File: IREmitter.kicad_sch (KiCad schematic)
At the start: 0 parts

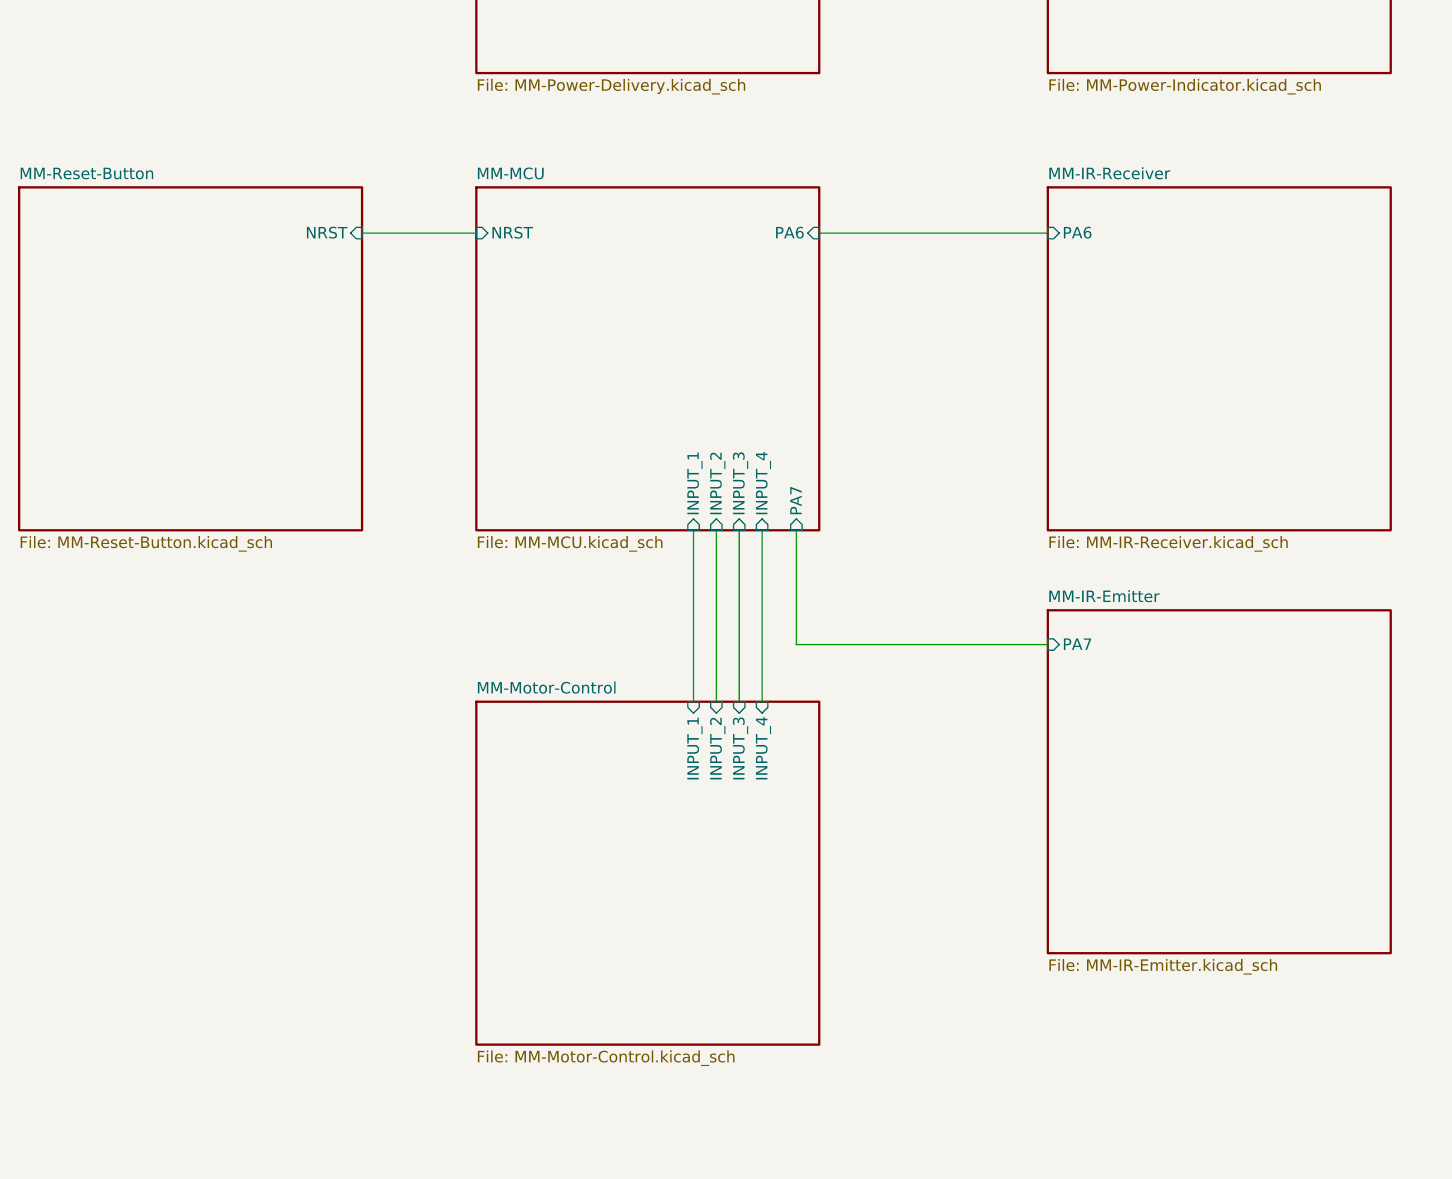
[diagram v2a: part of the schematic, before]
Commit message: redid the 4 emitters receivers, fixed orientation of LEDS and going to continue adding footprints and replace the 60ohm resistors with 300ohm ones
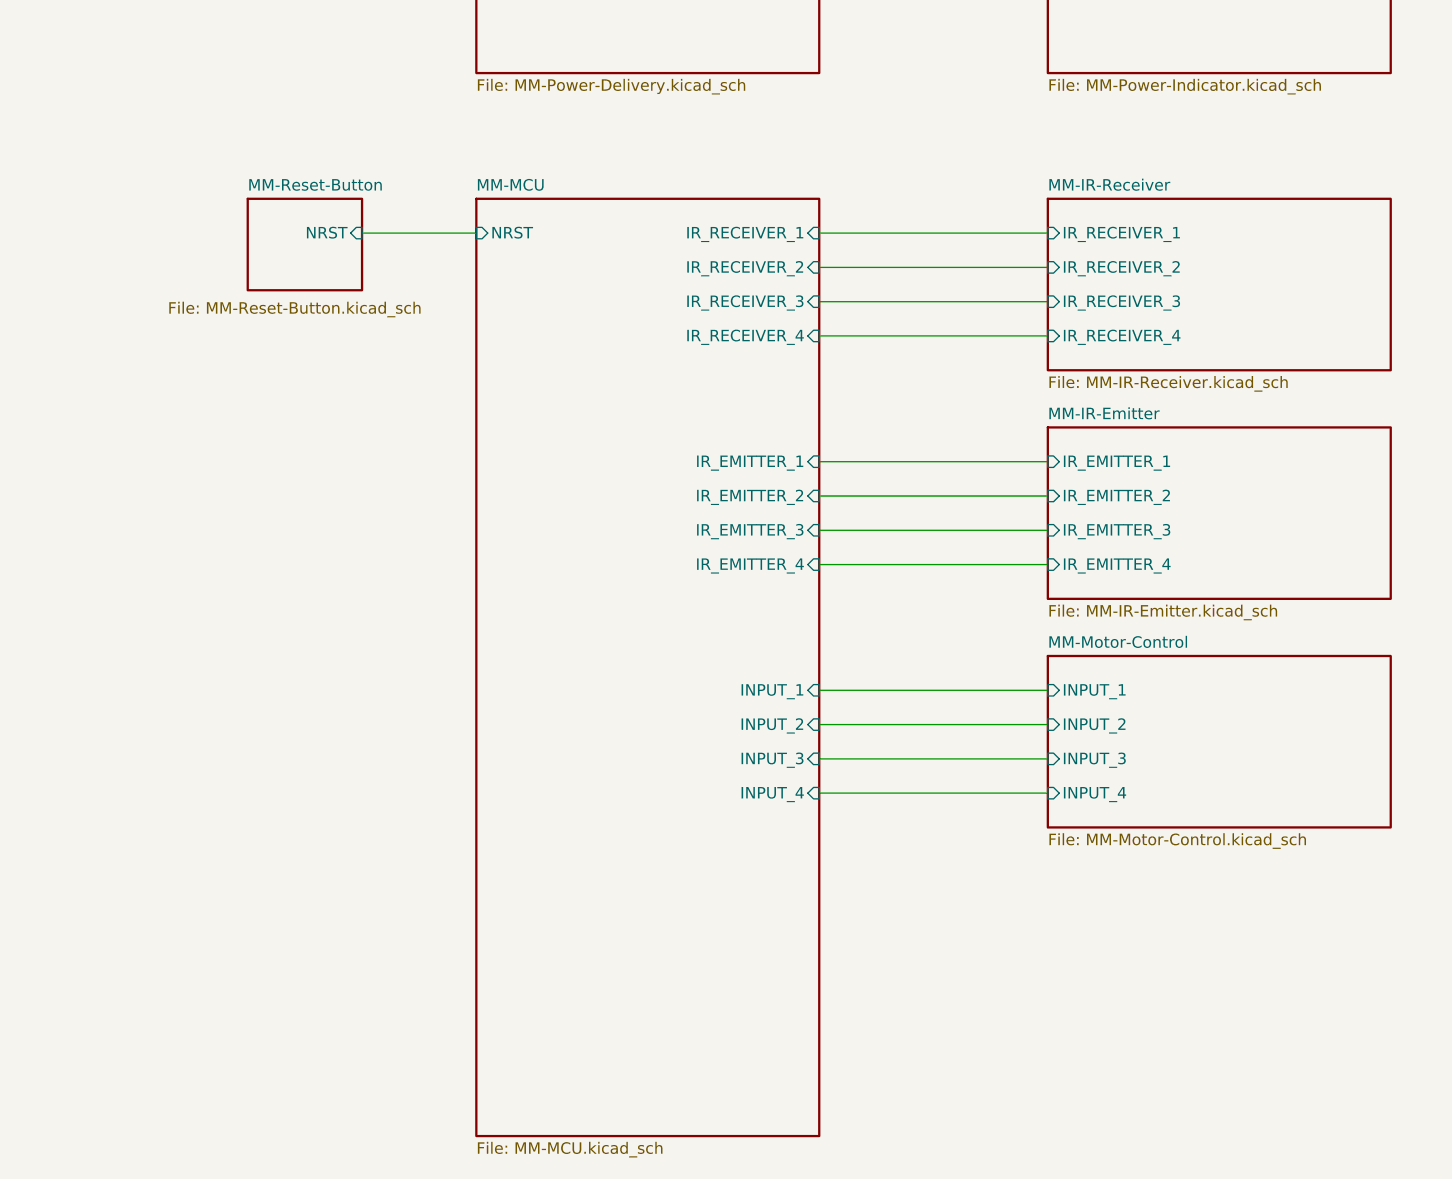
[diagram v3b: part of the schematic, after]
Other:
- sheet MM-IR-Emitter ports: added IR_EMITTER_1, IR_EMITTER_2, IR_EMITTER_3, IR_EMITTER_4; removed PA7
- sheet MM-IR-Receiver ports: added IR_RECEIVER_1, IR_RECEIVER_2, IR_RECEIVER_3, IR_RECEIVER_4; removed PA6
- sheet MM-MCU ports: added IR_EMITTER_1, IR_EMITTER_2, IR_EMITTER_3, IR_EMITTER_4, IR_RECEIVER_1, IR_RECEIVER_2, IR_RECEIVER_3, IR_RECEIVER_4; removed PA6, PA7

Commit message: PCB tentative finished
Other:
- added sheet Programming Header (prog_header.kicad_sch)
- sheet MM-MCU ports: added SWCLK, SWDIO; removed none
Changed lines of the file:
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@@
 	(generator_version "9.0")
 	(paper "A2")
+	(junction
+		(at 228.6 93.98)
+		(diameter 0)
+		(color 0 0 0 0)
+	)
+	(wire
+		(pts
+			(xy 215.9 115.57) (xy 228.6 115.57)
+		)
+		(stroke
+			(width 0)
+			(type default)
+		)
+	)
 	(wire
 		(pts
@@
 	(wire
 		(pts
+			(xy 215.9 113.03) (xy 215.9 106.68)
+		)
+		(stroke
+			(width 0)
+			(type default)
+		)
+	)
+	(wire
+		(pts
 			(xy 266.7 93.98) (xy 292.1 93.98)
 		)
@@
 	(wire
 		(pts
+			(xy 215.9 118.11) (xy 228.6 118.11)
+		)
+		(stroke
+			(width 0)
+			(type default)
+		)
+	)
+	(wire
+		(pts
 			(xy 215.9 93.98) (xy 228.6 93.98)
 		)
@@
 		(pts
 			(xy 266.7 97.79) (xy 292.1 97.79)
+		)
+		(stroke
+			(width 0)
+			(type default)
+		)
+	)
+	(wire
+		(pts
+			(xy 215.9 106.68) (xy 228.6 93.98)
 		)
 		(stroke
@@
 		)
 		(property "Sheetfile" "MM-Reset-Button.kicad_sch"
-			(at 194.31 101.6 0)
+			(at 185.42 101.6 0)
 			(effects
 				(font
@@
 			)
 		)
+		(pin "SWDIO" input
+			(at 228.6 115.57 180)
+			(effects
+				(font
+					(size 1.27 1.27)
+				)
+				(justify left)
+			)
+		)
+		(pin "SWCLK" input
+			(at 228.6 118.11 180)
+			(effects
+				(font
+					(size 1.27 1.27)
+				)
+				(justify left)
+			)
+		)
 		(instances
 			(project "IREmitter"
@@
 				)
 			)
+		)
+	)
+	(sheet
+		(at 177.8 109.22)
+		(size 38.1 20.32)
+		(exclude_from_sim no)
+		(in_bom yes)
+		(on_board yes)
+		(dnp no)
+		(fields_autoplaced yes)
+		(stroke
+			(width 0.1524)
+			(type solid)
+		)
+		(fill
+			(color 0 0 0 0.0000)
+		)
+		(property "Sheetname" "Programming Header"
+			(at 177.8 108.5084 0)
+			(effects
+				(font
+					(size 1.27 1.27)
+				)
+				(justify left bottom)
+			)
+		)
+		(property "Sheetfile" "prog_header.kicad_sch"
+			(at 177.8 130.1246 0)
+			(effects
+				(font
+					(size 1.27 1.27)
+				)
+				(justify left top)
+			)
+		)
+		(pin "NRST" input
+			(at 215.9 113.03 0)
+			(effects
+				(font
+					(size 1.27 1.27)
+				)
+				(justify right)
+			)
+		)
+		(pin "SWDIO" input
+			(at 215.9 115.57 0)
+			(effects
+				(font
+					(size 1.27 1.27)
+				)
+				(justify right)
+			)
+		)
+		(pin "SWCLK" input
+			(at 215.9 118.11 0)
+			(effects
+				(font
+					(size 1.27 1.27)
+				)
+				(justify right)
+			)
+		)
+		(instances
+			(project "IREmitter"
+				(path "/d311851a-8b0b-4acf-b2e7-1b968b2adbe7"
+					(page "9")
+				)
+			)
